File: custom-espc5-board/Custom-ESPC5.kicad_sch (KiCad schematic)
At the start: 52 parts, among them J1 Screw_Terminal_01x02, J10 Barrel_Jack, J12 Conn_01x05, J13 Conn_01x05, J4 USB_C_Receptacle_USB2.0_14P, J5 Conn_01x03, J6 Screw_Terminal_01x03, SW1 SW_Nidec_CAS-120A1, SW2 SW_Push, SW3 SW_Push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

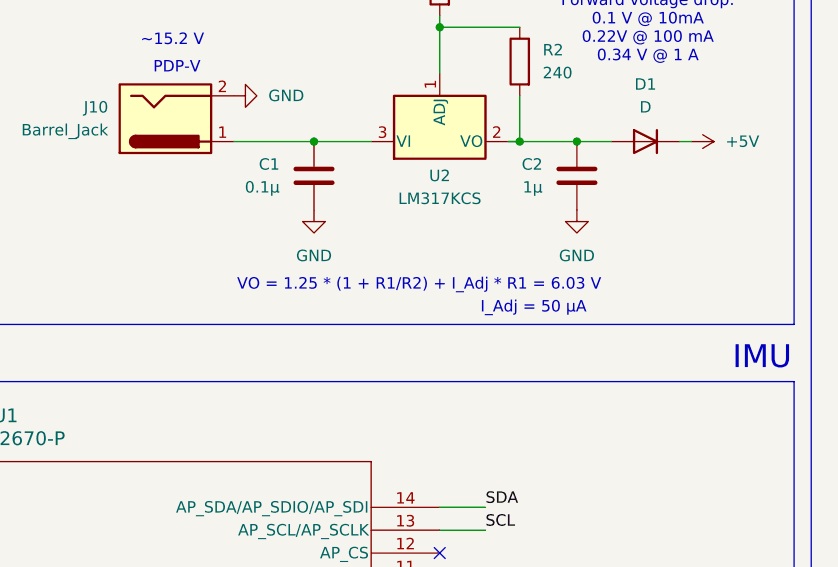
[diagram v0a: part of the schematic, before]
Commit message: Changed voltage regulator footprints and schematic
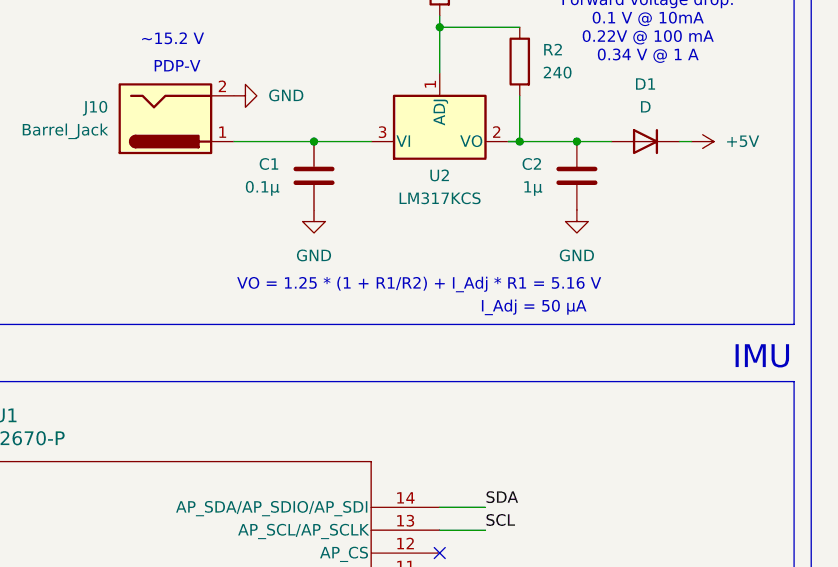
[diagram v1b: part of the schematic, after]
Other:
- note added: "VO = 1.25 * (1 + R1/R2) + I_Adj * R1 = 5.16 V"
- note removed: "VO = 1.25 * (1 + R1/R2) + I_Adj * R1 = 6.03 V"
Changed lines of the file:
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@@
 		)
 	)
-	(text "VO = 1.25 * (1 + R1/R2) + I_Adj * R1 = 6.03 V\n"
+	(text "VO = 1.25 * (1 + R1/R2) + I_Adj * R1 = 5.16 V\n"
 		(exclude_from_sim no)
 		(at 496.824 365.252 0)

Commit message: Changed voltage regulator footprints and schematic
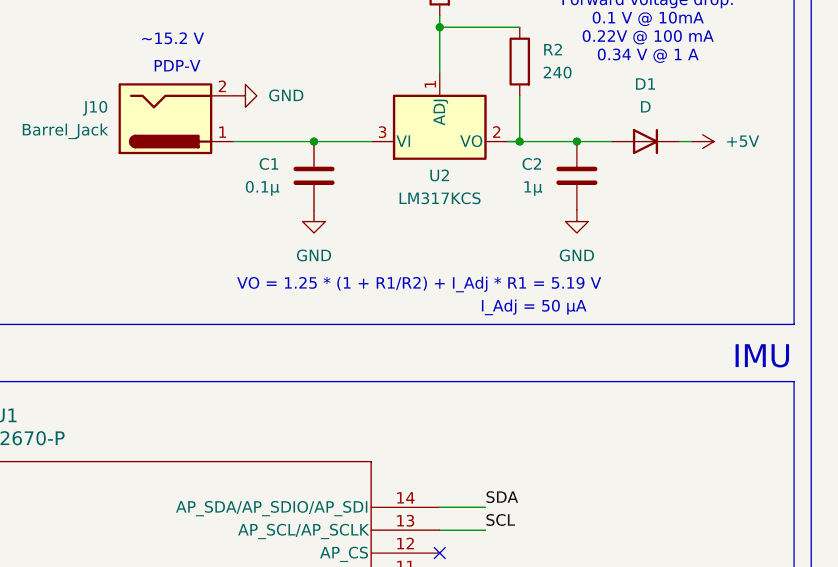
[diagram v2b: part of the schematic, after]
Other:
- note added: "VO = 1.25 * (1 + R1/R2) + I_Adj * R1 = 5.19 V"
- note removed: "VO = 1.25 * (1 + R1/R2) + I_Adj * R1 = 5.16 V"
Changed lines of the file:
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@@
 		)
 	)
-	(text "VO = 1.25 * (1 + R1/R2) + I_Adj * R1 = 5.16 V\n"
+	(text "VO = 1.25 * (1 + R1/R2) + I_Adj * R1 = 5.19 V\n"
 		(exclude_from_sim no)
 		(at 496.824 365.252 0)
